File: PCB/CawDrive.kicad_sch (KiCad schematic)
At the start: 43 parts, among them CN1 WAFER-SH1.0-6PWB, CN2 WAFER-SH1.0-6PWB, U1 AS5047P-ATSM, U3 TCAN1044DRBRQ1, U4 STM32G474RETx, U5 WAFER-SH1.0-2PWB, U6 WAFER-SH1.0-2PWB, X1 CSTNE16M0V530000R0

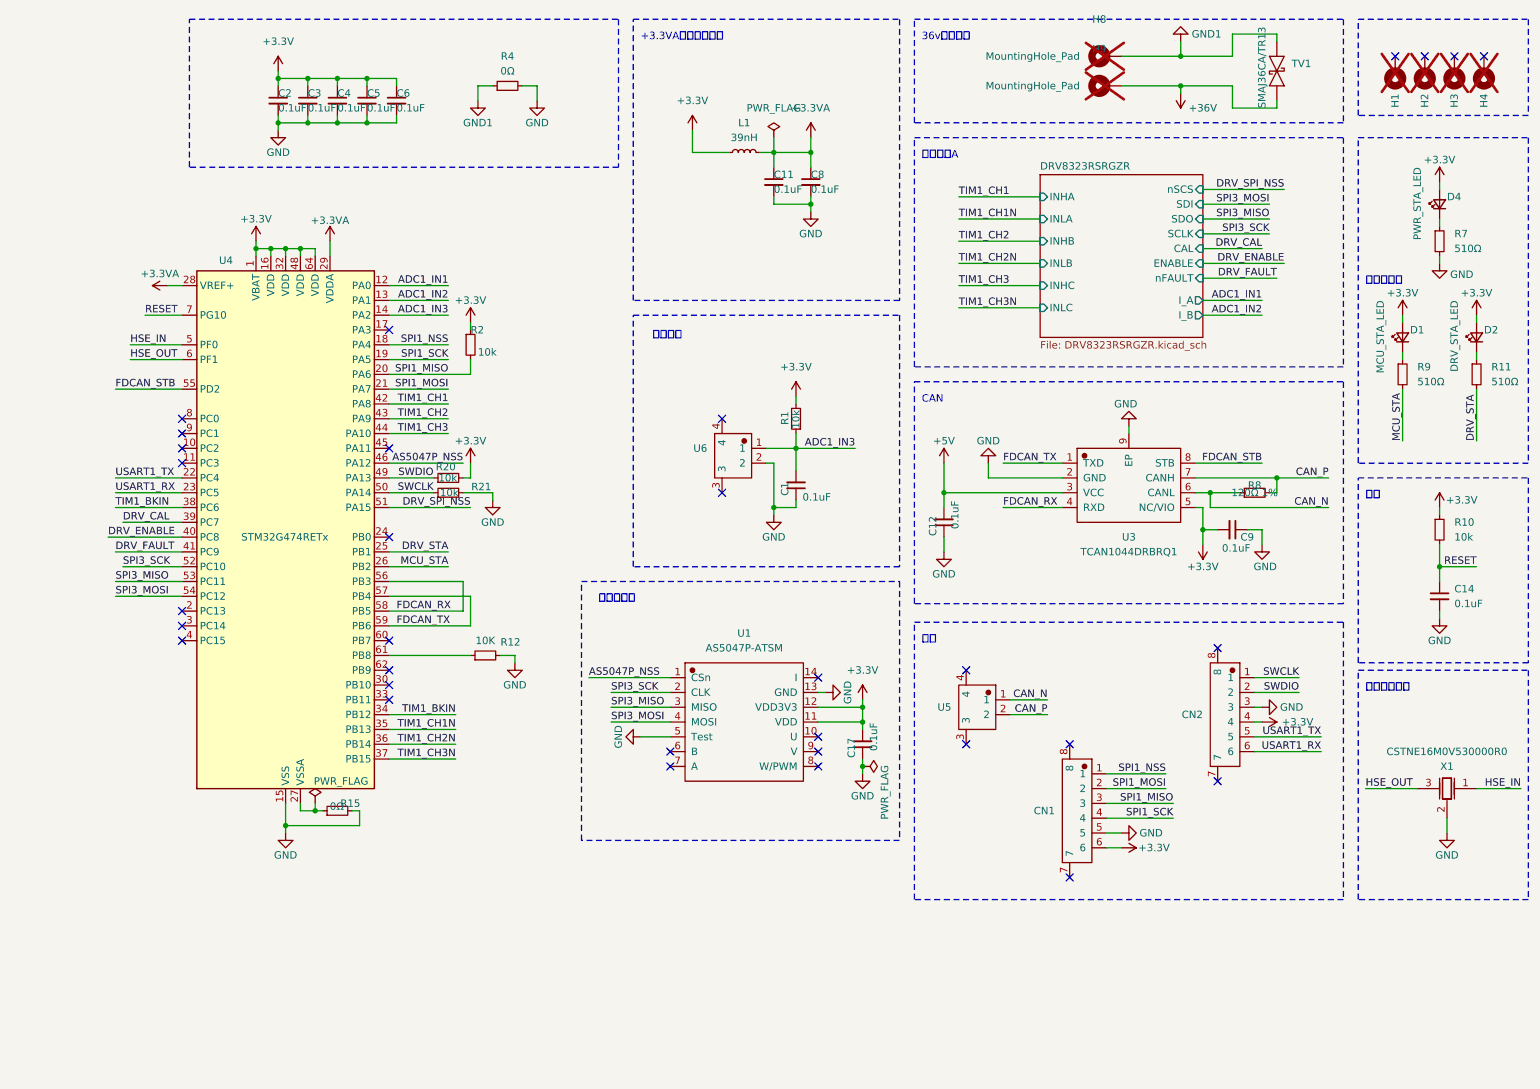
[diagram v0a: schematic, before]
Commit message: 升级V2版，支持3路电流采样以及霍尔传感器
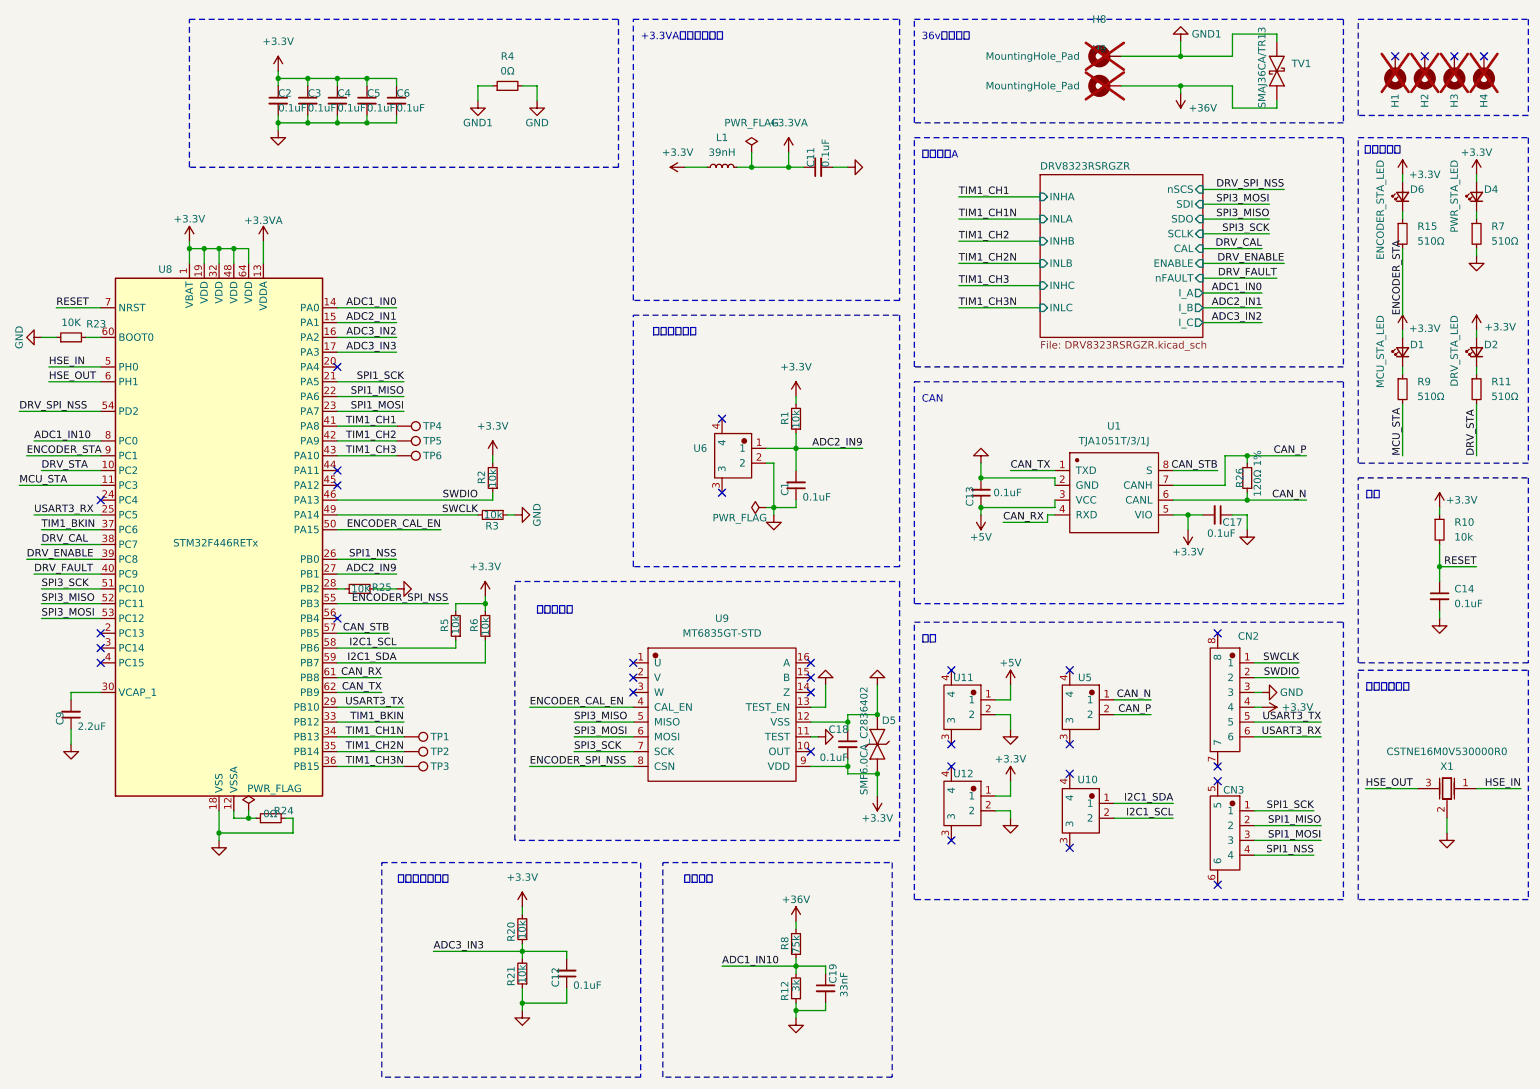
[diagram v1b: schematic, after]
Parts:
- removed C8: 0.1uF, Capacitor_SMD:C_0402_1005Metric_Pad0.74x0.62mm_HandSolder, symbol Device:C_Small
- removed CN1: WAFER-SH1.0-6PWB, Rick_Connector:CONN-SMD_6P-P1.00_XUNPU_WAFER-SH1.0-6PWB, symbol Rick_Connector:WAFER-SH1.0-6PWB
- removed U1: AS5047P-ATSM, Rick_Sensor:AS5047P-ATSM, symbol Rick_Sensor:AS5047P-ATSM
- removed U3: TCAN1044DRBRQ1, Rick_CAN:TCAN1044DRBRQ1_DFN-8_L3.0-W3.0-P0.65-TL-EP2.4, symbol Rick_CAN:TCAN1044DRBRQ1
- removed U4: STM32G474RETx, Package_QFP:LQFP-64_10x10mm_P0.5mm, symbol MCU_ST_STM32G4:STM32G474RETx
- added C13, C18: 0.1uF, Capacitor_SMD:C_0402_1005Metric_Pad0.74x0.62mm_HandSolder, symbol Device:C_Small
- added C19: 33nF, Capacitor_SMD:C_0402_1005Metric_Pad0.74x0.62mm_HandSolder, symbol Device:C_Small
- added CN3: WAFER-SH1.0-4PWB, Rick_Connector:CONN-SMD_4P-P1.00_WAFER-SH1.0-4PWB, symbol Rick_Connector:WAFER-SH1.0-4PWB
- added D5: SMF6.0CA_C2836402, Rick_Diode:SMF6.0CA_SOD-123FL_L2.8-W1.8-LS3.7-BI, symbol Rick_Diode:SMF6.0CA
- added D6: ENCODER_STA_LED, LED_SMD:LED_0402_1005Metric_Pad0.77x0.64mm_HandSolder, symbol Device:LED_Small
- added R23, R25: 10K, Resistor_SMD:R_0402_1005Metric_Pad0.72x0.64mm_HandSolder, symbol Device:R_Small
- added R24: 0Ω, Resistor_SMD:R_0402_1005Metric_Pad0.72x0.64mm_HandSolder, symbol Device:R_Small
- added R26: 120Ω 1%, Resistor_SMD:R_0402_1005Metric_Pad0.72x0.64mm_HandSolder, symbol Device:R_Small
- added R3, R5, R6: 10k, Resistor_SMD:R_0402_1005Metric_Pad0.72x0.64mm_HandSolder, symbol Device:R_Small
- added TP1, TP2, TP3, TP4, TP5, TP6: TestPoint, TestPoint:TestPoint_Pad_D1.0mm, symbol Connector:TestPoint
- added U1: TJA1051T/3/1J, Rick_CAN:TJA1051T31J_SOIC-8_L4.9-W3.9-P1.27-LS6.0-BL, symbol Rick_CAN:TJA1051T/3/1J
- added U10, U11, U12: WAFER-SH1.0-2PWB, Rick_Connector:CONN-SMD_2P-P1.00_XUNPU_WAFER-SH1.0-2PWB, symbol Rick_Connector:WAFER-SH1.0-2PWB
- added U8: STM32F446RETx, Package_QFP:LQFP-64_10x10mm_P0.5mm, symbol MCU_ST_STM32F4:STM32F446RETx
- added U9: MT6835GT-STD, Rick_Sensor:MT6835GT-STD, symbol Rick_Sensor:MT6835GT-STD
- C9: value 0.1uF -> 2.2uF
- R12: value 10K -> 3k
- R15: value 0Ω -> 510Ω
- R8: value 120Ω 1% -> 75k
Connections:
- net +3.3V: now also R2.2, C18.2, D5.1, D6.2 (A), R5.2, R6.2, U1.5 (VIO), U12.1, U8.1 (VBAT), U8.19 (VDD), U8.32 (VDD), U8.48 (VDD), U8.64 (VDD), U9.9 (VDD); no longer C9.2, R2.1
- net +3.3VA: now also U8.13 (VDDA)
- net +36V: now also R8.2
- net +5V: now also C13.1, U1.3 (VCC), U11.1; no longer C12.2
- net CAN_N: now also R26.1, U1.6 (CANL); no longer R8.1
- net CAN_P: now also R26.2, U1.7 (CANH); no longer R8.2
- net DRV_CAL: now also U8.38 (PC7)
- net DRV_ENABLE: now also U8.39 (PC8)
- net DRV_FAULT: now also U8.40 (PC9)
- net DRV_SPI_NSS: now also U8.54 (PD2)
- net DRV_STA: now also U8.10 (PC2)
- net GND: now also R12.1, R21.1, C13.2, C18.1, C19.2, D5.2, R23.1, R24.2, R25.2, R3.1, U1.2 (GND), U11.2, U12.2, U8.18 (VSS), U8.31 (VSS), U8.47 (VSS), U8.63 (VSS), U9.11 (TEST), U9.12 (VSS), U9.13 (TEST_EN); no longer R12.2, R15.2, R21.2
- net HSE_IN: now also U8.5 (PH0)
- net HSE_OUT: now also U8.6 (PH1)
- net MCU_STA: now also U8.11 (PC3)
- net RESET: now also U8.7 (NRST)
- net SPI1_MISO: now also CN3.2, U8.22 (PA6); no longer R2.2
- net SPI1_MOSI: now also CN3.3, U8.23 (PA7)
- net SPI1_NSS: now also CN3.4, U8.26 (PB0)
- net SPI1_SCK: now also CN3.1, U8.21 (PA5)
- net SPI3_MISO: now also U8.52 (PC11), U9.5 (MISO)
- net SPI3_MOSI: now also U8.53 (PC12), U9.6 (MOSI)
- net SPI3_SCK: now also U8.51 (PC10), U9.7 (SCK)
- net SWCLK: now also R3.2, U8.49 (PA14); no longer R21.1
- net SWDIO: now also R2.1, U8.46 (PA13); no longer R20.1
- net TIM1_BKIN: now also U8.33 (PB12), U8.37 (PC6)
- net TIM1_CH1: now also TP4.1, U8.41 (PA8)
- net TIM1_CH1N: now also TP1.1, U8.34 (PB13)
- net TIM1_CH2: now also TP5.1, U8.42 (PA9)
- net TIM1_CH2N: now also TP2.1, U8.35 (PB14)
- net TIM1_CH3: now also TP6.1, U8.43 (PA10)
- net TIM1_CH3N: now also TP3.1, U8.36 (PB15)
- net at R15.1: now also D6.1 (K)
- net ADC1_IN3 renamed ADC2_IN9
- net ADC2_IN9: now also U8.27 (PB1)
- net USART1_RX renamed USART3_RX
- net USART3_RX: now also U8.25 (PC5)
- net USART1_TX renamed USART3_TX
- net USART3_TX: now also U8.29 (PB10)
- new net: C9.2, U8.30 (VCAP_1)
- new net: R24.1, U8.12 (VSSA)
- new net: R25.1, U8.28 (PB2)
- new net: R23.2, U8.60 (BOOT0)
- new net ADC1_IN0: U8.14 (PA0)
- new net ADC1_IN10: C19.1, R12.2, R8.1, U8.8 (PC0)
- new net ADC2_IN1: U8.15 (PA1)
- new net ADC3_IN2: U8.16 (PA2)
- new net ADC3_IN3: C12.2, R20.1, R21.2, U8.17 (PA3)
- new net CAN_RX: U1.4 (RXD), U8.61 (PB8)
- new net CAN_STB: U1.8 (S), U8.57 (PB5)
- new net CAN_TX: U1.1 (TXD), U8.62 (PB9)
- new net ENCODER_CAL_EN: U8.50 (PA15), U9.4 (CAL_EN)
- new net ENCODER_SPI_NSS: U8.55 (PB3), U9.8 (CSN)
- new net ENCODER_STA: R15.2, U8.9 (PC1)
- new net I2C1_SCL: R5.1, U10.2, U8.58 (PB6)
- new net I2C1_SDA: R6.1, U10.1, U8.59 (PB7)
- no-connect marks 32 -> 33
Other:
- sheet DRV8323RSRGZR ports: added I_C; removed none
- note added: "母线电压"
- note added: "电机温度采样"
- note added: "驱动器温度采样"
- note removed: "温度采样"
- moved on the sheet: C11, CN2, D1, D2, D4, L1, R11, R7, R9, U5

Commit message: 增加测试点PC13引脚
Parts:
- added TP7: TestPoint, TestPoint:TestPoint_Pad_D1.0mm, symbol Connector:TestPoint
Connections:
- net at U8.2 (PC13): now also TP7.1
- no-connect marks 33 -> 32
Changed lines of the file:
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@@
 	)
 	(no_connect
-		(at 38.1 118.11)
-	)
-	(no_connect
 		(at 265.43 19.05)
 	)
@@
 	(wire
 		(pts
+			(xy 36.83 118.11) (xy 38.1 118.11)
+		)
+		(stroke
+			(width 0)
+			(type default)
+		)
+	)
+	(wire
+		(pts
 			(xy 212.09 149.86) (xy 222.25 149.86)
 		)
@@
 					(unit 1)
 				)
+			)
+		)
+	)
+	(symbol
+		(lib_id "Connector:TestPoint")
+		(at 36.83 118.11 90)
+		(mirror x)
+		(unit 1)
+		(exclude_from_sim no)
+		(in_bom yes)
+		(on_board yes)
+		(dnp no)
+		(property "Reference" "TP7"
+			(at 32.258 118.11 90)
+			(effects
+				(font
+					(size 1.27 1.27)
+				)
+				(justify left)
+			)
+		)
+		(property "Value" "TestPoint"
+			(at 32.004 118.11 90)
+			(effects
+				(font
+					(size 1.27 1.27)
+				)
+				(justify left)
+				(hide yes)
+			)
+		)
+		(property "Footprint" "TestPoint:TestPoint_Pad_D1.0mm"
+			(at 36.83 123.19 0)
+			(effects
+				(font
+					(size 1.27 1.27)
+				)
+				(hide yes)
+			)
+		)
+		(property "Datasheet" "~"
+			(at 36.83 123.19 0)
+			(effects
+				(font
+					(size 1.27 1.27)
+				)
+				(hide yes)
+			)
+		)
+		(property "Description" "test point"
+			(at 36.83 118.11 0)
+			(effects
+				(font
+					(size 1.27 1.27)
+				)
+				(hide yes)
+			)
+		)
+		(pin "1"
+		)
+		(instances
+			(project "CawDrive"
+				(path "/80524a83-b783-469c-b956-da06086e2ffd"
+					(reference "TP7")
+					(unit 1)
+				)

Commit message: 更新README
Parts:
- C19: value 33nF -> 0.1uF/50V
- R1, R20: value 10k -> 10k 1%
- R12: value 3k -> 3k 1%
- R21: value 10k -> NTC
- R8: value 75k -> 75k 1%
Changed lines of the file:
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@@
 			)
 		)
-		(property "Value" "10k"
-			(at 157.48 79.756 90)
+		(property "Value" "10k 1%"
+			(at 166.116 80.772 0)
 			(effects
 				(font
@@
 			)
 		)
-		(property "Value" "10k"
-			(at 110.49 167.386 90)
+		(property "Value" "10k 1%"
+			(at 119.126 168.402 0)
 			(effects
 				(font
@@
 			)
 		)
-		(property "Value" "75k"
-			(at 157.48 169.926 90)
+		(property "Value" "75k 1%"
+			(at 166.116 171.196 0)
 			(effects
 				(font
@@
 		(dnp no)
 		(property "Reference" "R12"
-			(at 155.575 177.8 90)
+			(at 159.258 177.038 90)
 			(effects
 				(font
@@
 			)
 		)
-		(property "Value" "3k"
-			(at 157.48 177.546 90)
+		(property "Value" "3k 1%"
+			(at 156.464 178.816 0)
 			(effects
 				(font
@@
 			)
 		)
-		(property "Value" "33nF"
+		(property "Value" "0.1uF/50V"
 			(at 165.735 178.435 90)
 			(effects
@@
 			)
 		)
-		(property "Value" "10k"
+		(property "Value" "NTC"
 			(at 110.49 175.006 90)
 			(effects

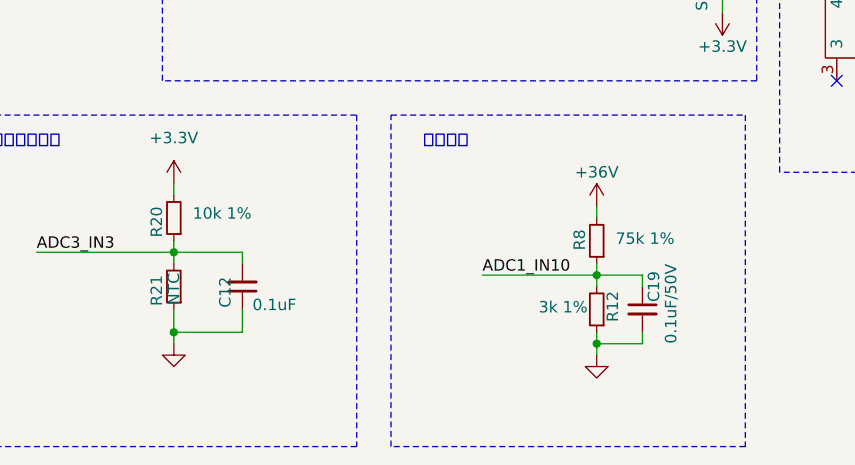
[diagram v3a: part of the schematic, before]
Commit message: 更新电阻精度，重新生成BOM
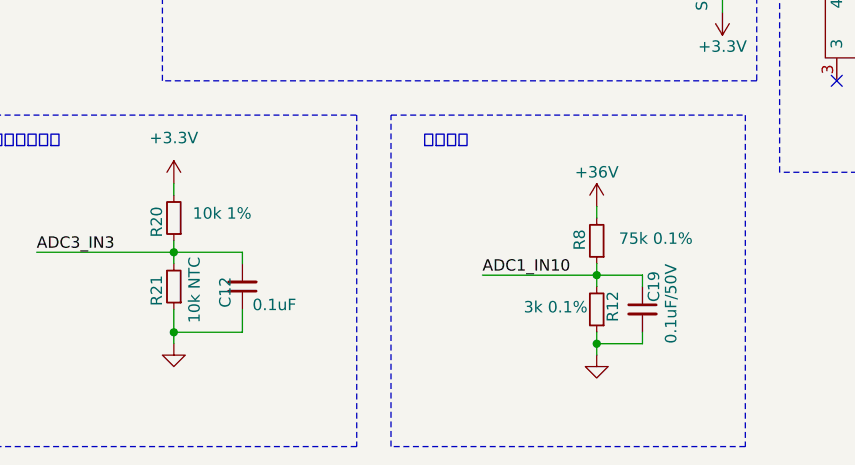
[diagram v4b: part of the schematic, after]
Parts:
- R12: value 3k 1% -> 3k 0.1%
- R21: value NTC -> 10k NTC
- R8: value 75k 1% -> 75k 0.1%
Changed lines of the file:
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@@
 			)
 		)
-		(property "Value" "75k 1%"
-			(at 166.116 171.196 0)
+		(property "Value" "75k 0.1%"
+			(at 168.148 171.196 0)
 			(effects
 				(font
@@
 			)
 		)
-		(property "Value" "3k 1%"
+		(property "Value" "3k 0.1%"
 			(at 156.464 178.816 0)
 			(effects
@@
 			)
 		)
-		(property "Value" "NTC"
-			(at 110.49 175.006 90)
+		(property "Value" "10k NTC"
+			(at 112.776 173.228 90)
 			(effects
 				(font

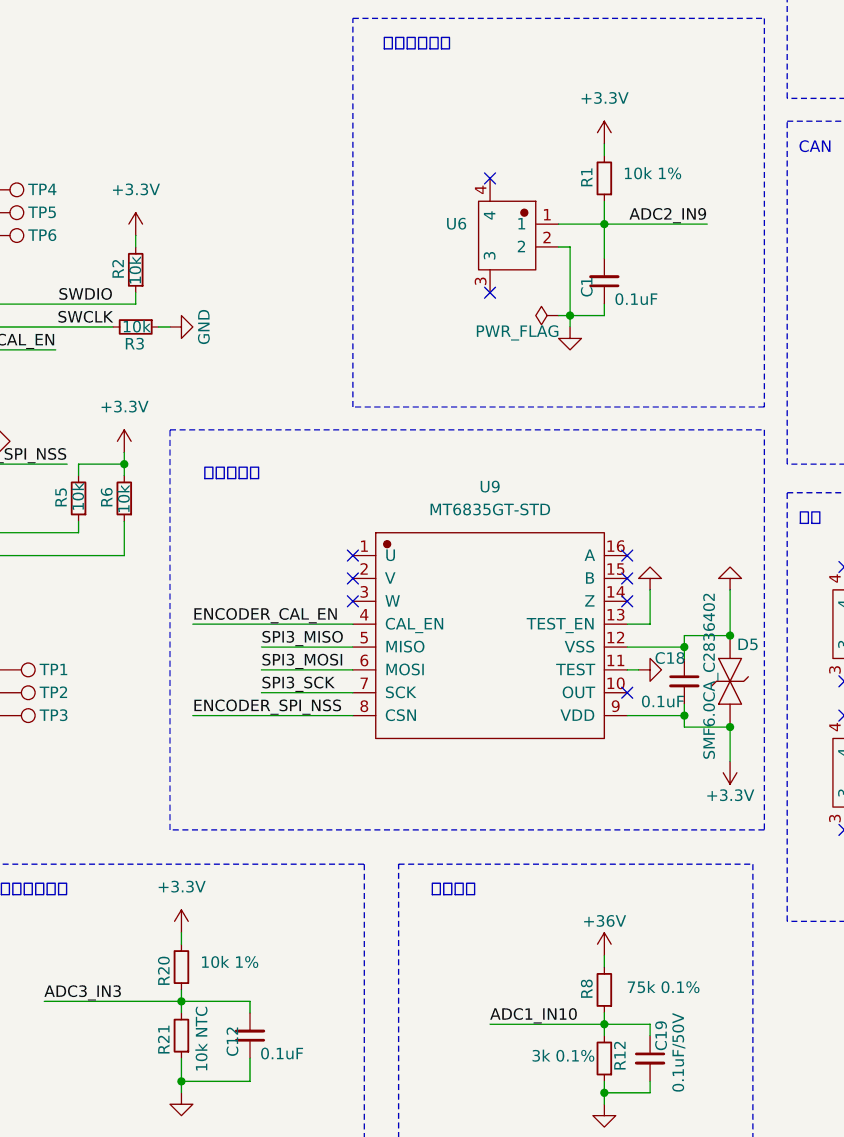
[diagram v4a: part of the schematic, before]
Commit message: 更新采样电阻精度，重新生成BOM
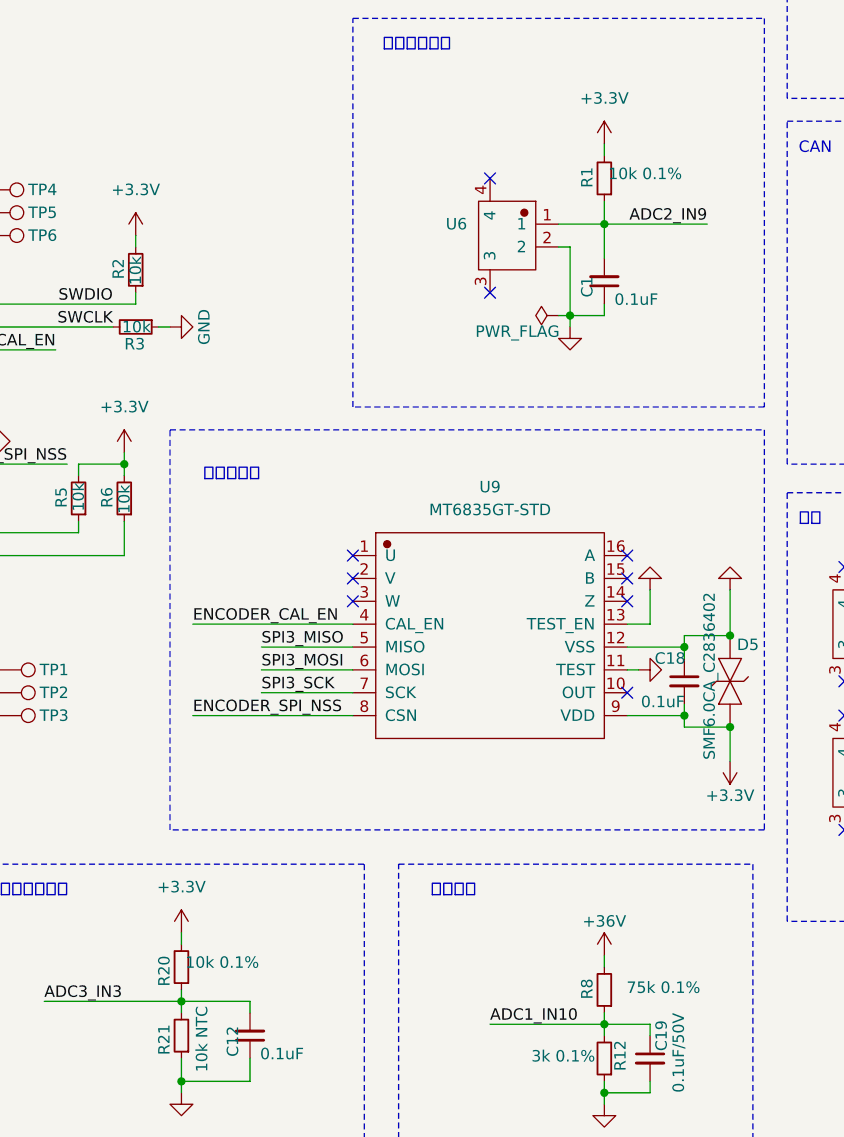
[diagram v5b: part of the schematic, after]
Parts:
- R1, R20: value 10k 1% -> 10k 0.1%
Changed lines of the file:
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@@
 			)
 		)
-		(property "Value" "10k 1%"
+		(property "Value" "10k 0.1%"
 			(at 166.116 80.772 0)
 			(effects
@@
 			)
 		)
-		(property "Value" "10k 1%"
+		(property "Value" "10k 0.1%"
 			(at 119.126 168.402 0)
 			(effects
